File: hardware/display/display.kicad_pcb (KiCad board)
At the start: 2 copper layers, 110 x 70 mm, 58 parts, among them J1 Conn_01x05_Male, J2 CANPWR, J3 CANGND, J4 RJ45, J5 RJ45, J6 Conn_02x03_Odd_Even, J7 DCDC-PWM, J8 DCDC-MEASURES, J9 display, Q1 BSS123, SW1 next, SW2 select, U1 2.048V, U2 AP63200WU, U3 PIC18F27Q84, U4 TLE9250VSJXUMA1, Y1 10Mhz

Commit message: WIP on diaplay PCB.
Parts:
- removed C10, C12: 22µ, Capacitor_SMD:C_1206_3216Metric_Pad1.33x1.80mm_HandSolder
- removed C11, C13, C7: 100nF, Capacitor_SMD:C_0805_2012Metric_Pad1.18x1.45mm_HandSolder
- removed C14: 100nF, local:C_filter_0805
- removed C2, C3: 4.7µ50V, Capacitor_SMD:C_1206_3216Metric_Pad1.33x1.80mm_HandSolder
- removed C4, C8: 100nF50V, Capacitor_SMD:C_0805_2012Metric_Pad1.18x1.45mm_HandSolder
- removed C5, C6: 22pF, Capacitor_THT:C_Disc_D3.8mm_W2.6mm_P2.50mm
- removed C9: 100p, Capacitor_SMD:C_0805_2012Metric_Pad1.18x1.45mm_HandSolder
- removed D1, D2: PMEG4005, Diode_SMD:D_SOD-123
- removed D3: SMBJ16A, Diode_SMD:D_SMB_Handsoldering
- removed F1, F2: MC011014, Fuse:Fuse_2920_7451Metric_Pad2.10x5.45mm_HandSolder
- removed J2: CANPWR, Connector_PinHeader_2.54mm:PinHeader_1x02_P2.54mm_Vertical
- removed J3: CANGND, Connector_PinHeader_2.54mm:PinHeader_1x02_P2.54mm_Vertical
- removed J4, J5: RJ45, local:RJ45_Amphenol_54602-x08_Horizontal_handsolder
- removed J6: Conn_02x03_Odd_Even, Connector_PinHeader_2.54mm:PinHeader_2x03_P2.54mm_Vertical
- removed J7: DCDC-PWM, Connector_PinHeader_2.54mm:PinHeader_2x05_P2.54mm_Vertical
- removed J8: DCDC-MEASURES, Connector_PinHeader_2.54mm:PinHeader_2x05_P2.54mm_Vertical
- removed J9: display, Connector_Harwin:Harwin_M20-7810345_2x03_P2.54mm_Vertical
- removed L1: 10µH, Inductor_SMD:L_12x12mm_H4.5mm
- removed Q1: BSS123, Package_TO_SOT_SMD:SOT-23
- removed R10: 8.1K, Resistor_THT:R_Axial_DIN0309_L9.0mm_D3.2mm_P12.70mm_Horizontal
- removed R11: 4K7, Resistor_SMD:R_0805_2012Metric_Pad1.20x1.40mm_HandSolder
- removed R12: 4K7, Resistor_THT:R_Axial_DIN0309_L9.0mm_D3.2mm_P12.70mm_Horizontal
- removed R13, R4, R5, R8: 10K, Resistor_SMD:R_0805_2012Metric_Pad1.20x1.40mm_HandSolder
- removed R14: 100K, Resistor_SMD:R_0805_2012Metric_Pad1.20x1.40mm_HandSolder
- removed R15, R16: 47k, Resistor_SMD:R_0805_2012Metric_Pad1.20x1.40mm_HandSolder
- removed R17: 22k, Resistor_SMD:R_0805_2012Metric_Pad1.20x1.40mm_HandSolder
- removed R18: 100, Resistor_SMD:R_0805_2012Metric_Pad1.20x1.40mm_HandSolder
- removed R2: 270k, Resistor_SMD:R_0805_2012Metric_Pad1.20x1.40mm_HandSolder
- removed R3, R7: 30k, Resistor_SMD:R_0805_2012Metric_Pad1.20x1.40mm_HandSolder
- removed R6: 157k, Resistor_SMD:R_0805_2012Metric_Pad1.20x1.40mm_HandSolder
- removed R9: 10K, Resistor_THT:R_Axial_DIN0309_L9.0mm_D3.2mm_P12.70mm_Horizontal
- removed SW1: next, Button_Switch_THT:Push_E-Switch_KS01Q01
- removed SW2: select, Button_Switch_THT:Push_E-Switch_KS01Q01
- removed U1: 2.048V, Package_TO_SOT_SMD:SOT-23
- removed U2: AP63200WU, Package_TO_SOT_SMD:TSOT-23-6
- removed U3: PIC18F27Q84, Package_SO:SOIC-28W_7.5x17.9mm_P1.27mm
- removed U4: TLE9250VSJXUMA1, Package_SO:SOIC-8_3.9x4.9mm_P1.27mm
- removed Y1: 10Mhz, Crystal:Crystal_HC18-U_Vertical
- added DI1: MCOB128064JX, LCDdisplays.mod:MCOB128064JX, F.Cu at (112.0, 105.0)
- H1, H2, H3, H4: value MountingHole -> 3.2mm
- J1: value Conn_01x05_Male -> Conn_02x03_Odd_Even; footprint Connector_PinHeader_2.54mm:PinHeader_1x05_P2.54mm_Horizontal -> harwin:M20-8750342
- moved C1 153.5 mm to (232.4, 43.2), turned to 0 degrees
- moved J1 46.6 mm to (140.0, 86.3)
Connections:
- C1 pad 2: Net-(C1-Pad2) -> +5V
- J1 pad 2: /PGD -> unconnected-(J1-Pad2)
- J1 pad 3: /PGC -> GND
- J1 pad 4: GND -> /~{RST_DISP}
- J1 pad 5: /MCLR -> /SDA
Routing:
- net +5V: track 306.6 -> 0.00 mm, vias 3 -> 0
- net BTN_IN: track 96.5 -> 0.00 mm, vias 1 -> 0
- net SDA: track 94.0 -> 0.00 mm, vias 1 -> 0
- net PWM_V: track 69.9 -> 0.00 mm, vias 2 -> 0
- net TH: track 66.2 -> 0.00 mm, vias 2 -> 0
- net /CANL: track 64.9 -> 0.00 mm
- net /PWM_OFF: track 62.8 -> 0.00 mm
- net /CANGND: track 61.5 -> 0.00 mm
- net /CANH: track 59.3 -> 0.00 mm
- net /PWM: track 58.6 -> 0.00 mm
- net /PWM_OK: track 57.2 -> 0.00 mm
- net AL1: track 56.1 -> 0.00 mm, vias 2 -> 0
- net Net-(C14-Pad1): track 55.3 -> 0.00 mm
- net /~{PAC_DOWN}: track 55.2 -> 0.00 mm, vias 2 -> 0
- net AL2: track 55.1 -> 0.00 mm, vias 2 -> 0
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- removed copper zone on F.Cu, net /CANGND
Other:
- outline, holes or cut-outs redrawn

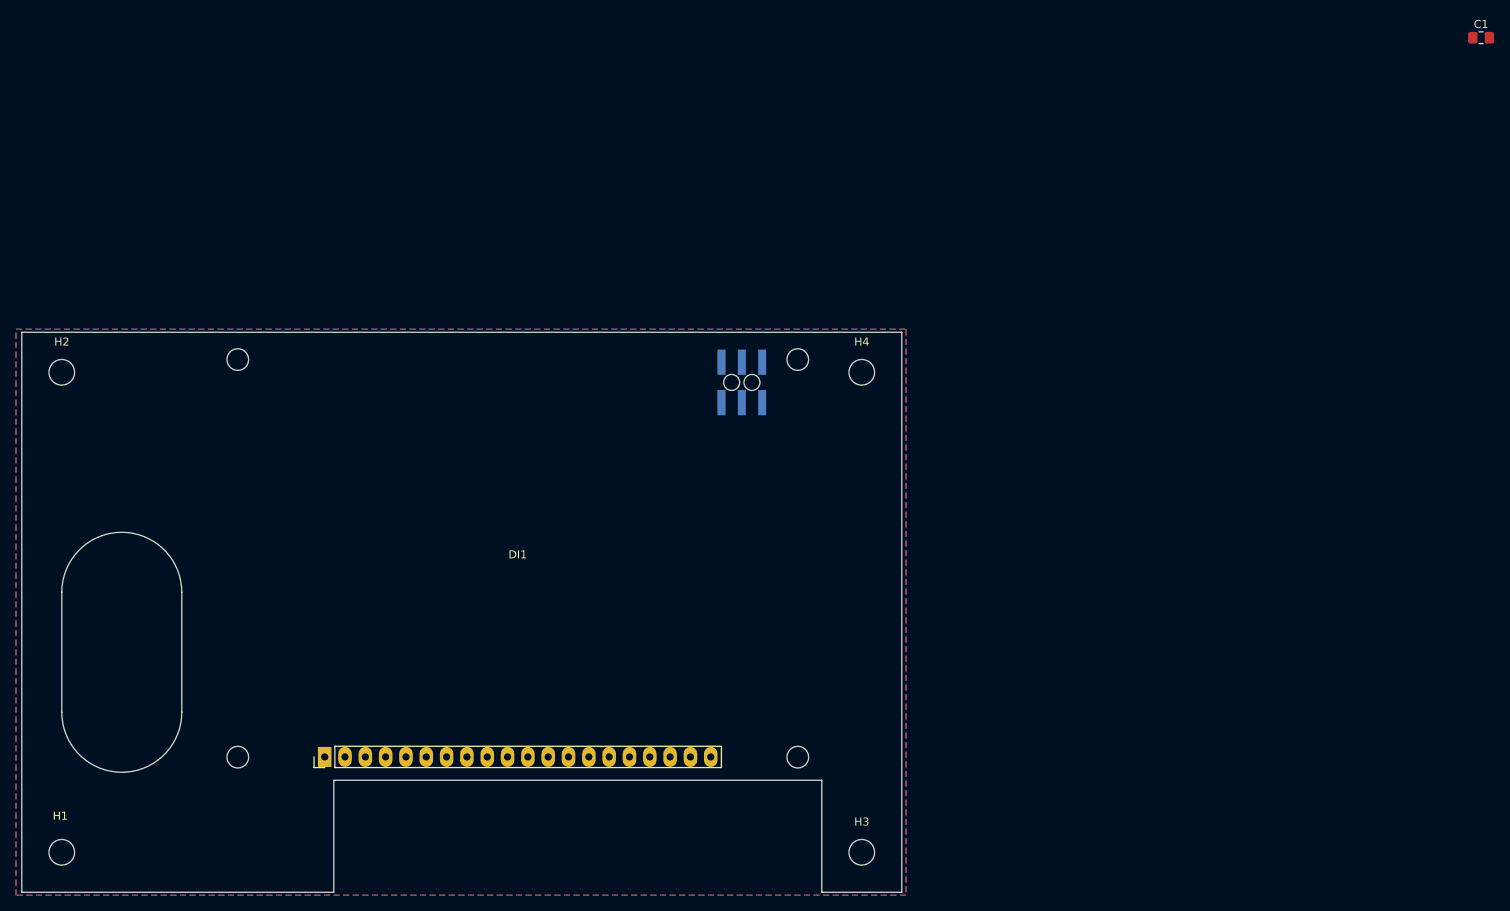
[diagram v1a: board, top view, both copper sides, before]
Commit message: Route display PCB. Adjust control for connector wiring changes.
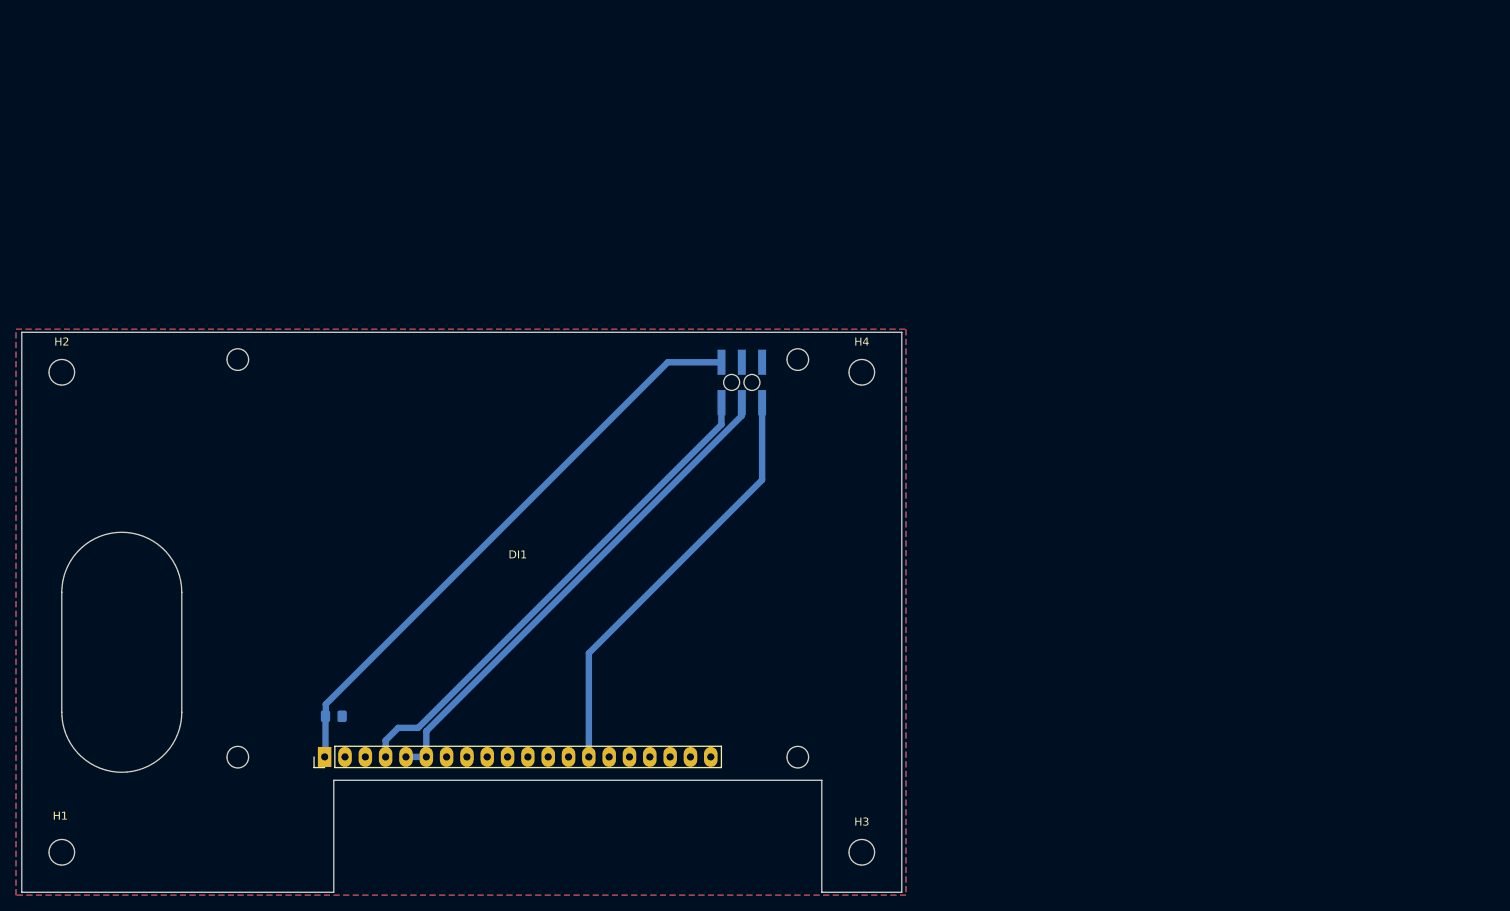
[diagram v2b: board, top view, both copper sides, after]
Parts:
- C1: moved to B.Cu
- moved C1 166.6 mm to (89.0, 128.0), turned to 180 degrees
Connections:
- J1 pad 4: /~{RST_DISP} -> /SCL
- J1 pad 6: /SCL -> /~{RST_DISP}
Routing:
- net +5V: track 0.00 -> 73.8 mm
- net /SDA: track 0.00 -> 63.2 mm
- net /SCL: track 0.00 -> 63.1 mm
- net /~{RST_DISP}: track 0.00 -> 53.3 mm
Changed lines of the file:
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@@
   (paper "A4")
   (layers
-    (0 "F.Cu" signal)
+    (0 "F.Cu" jumper)
     (31 "B.Cu" signal)
     (32 "B.Adhes" user "B.Adhesive")
@@
     (pad "" np_thru_hole circle locked (at 0 0) (size 3.2 3.2) (drill 3.2) (layers *.Cu *.Mask))
   )
-  (footprint "Capacitor_SMD:C_0805_2012Metric_Pad1.18x1.45mm_HandSolder" (layer "F.Cu")
-    (at 232.41 43.18)
-    (descr "Capacitor SMD 0805 (2012 Metric), square (rectangular) end terminal, IPC_7351 nominal with elongated pad for handsoldering. (Body size source: IPC-SM-782 page 76, https://www.pcb-3d.com/wordpress/wp-content/uploads/ipc-sm-782a_amendment_1_and_2.pdf, https://docs.google.com/spreadsheets/d/1BsfQQcO9C6DZCsRaXUlFlo91Tg2WpOkGARC1WS5S8t0/edit?usp=sharing), generated with kicad-footprint-generator")
-    (tags "capacitor handsolder")
-    (property "Sheetfile" "display.kicad_sch")
-    (property "Sheetname" "")
-    (attr smd)
-    (fp_text reference "C1" (at 0 -1.68) (layer "F.SilkS")
-      (effects (font (size 1 1) (thickness 0.15)))
-    )
-    (fp_text value "100nF" (at 0 1.68) (layer "F.Fab")
-      (effects (font (size 1 1) (thickness 0.15)))
-    )
-    (fp_text user "${REFERENCE}" (at 0 0) (layer "F.Fab")
-      (effects (font (size 0.5 0.5) (thickness 0.08)))
-    )
-    (fp_line (start -0.261252 0.735) (end 0.261252 0.735) (layer "F.SilkS") (width 0.12))
-    (fp_line (start -0.261252 -0.735) (end 0.261252 -0.735) (layer "F.SilkS") (width 0.12))
-    (fp_line (start -1.88 0.98) (end -1.88 -0.98) (layer "F.CrtYd") (width 0.05))
-    (fp_line (start 1.88 -0.98) (end 1.88 0.98) (layer "F.CrtYd") (width 0.05))
-    (fp_line (start 1.88 0.98) (end -1.88 0.98) (layer "F.CrtYd") (width 0.05))
-    (fp_line (start -1.88 -0.98) (end 1.88 -0.98) (layer "F.CrtYd") (width 0.05))
-    (fp_line (start 1 -0.625) (end 1 0.625) (layer "F.Fab") (width 0.1))
-    (fp_line (start 1 0.625) (end -1 0.625) (layer "F.Fab") (width 0.1))
-    (fp_line (start -1 0.625) (end -1 -0.625) (layer "F.Fab") (width 0.1))
-    (fp_line (start -1 -0.625) (end 1 -0.625) (layer "F.Fab") (width 0.1))
-    (pad "1" smd roundrect (at -1.0375 0) (size 1.175 1.45) (layers "F.Cu" "F.Paste" "F.Mask") (roundrect_rratio 0.212766)
-      (net 1 "GND") (pintype "passive"))
-    (pad "2" smd roundrect (at 1.0375 0) (size 1.175 1.45) (layers "F.Cu" "F.Paste" "F.Mask") (roundrect_rratio 0.212766)
-      (net 2 "+5V") (pintype "passive"))
-    (model "${KICAD6_3DMODEL_DIR}/Capacitor_SMD.3dshapes/C_0805_2012Metric.wrl"
-      (offset (xyz 0 0 0))
-      (scale (xyz 1 1 1))
-      (rotate (xyz 0 0 0))
-    )
-  )
   (footprint "harwin:M20-8750342" (layer "B.Cu")
     (at 140 86.27 -90)
@@
       (net 1 "GND") (pinfunction "Pin_3") (pintype "passive"))
     (pad "4" smd rect (at 2.525 2.54 270) (size 3.15 1) (layers "B.Cu" "B.Paste" "B.Mask")
-      (net 10 "/~{RST_DISP}") (pinfunction "Pin_4") (pintype "passive"))
+      (net 8 "/SCL") (pinfunction "Pin_4") (pintype "passive"))
     (pad "5" smd rect (at 2.525 0 270) (size 3.15 1) (layers "B.Cu" "B.Paste" "B.Mask")
       (net 9 "/SDA") (pinfunction "Pin_5") (pintype "passive"))
     (pad "6" smd rect (at 2.525 -2.54 270) (size 3.15 1) (layers "B.Cu" "B.Paste" "B.Mask")
-      (net 8 "/SCL") (pinfunction "Pin_6") (pintype "passive"))
+      (net 10 "/~{RST_DISP}") (pinfunction "Pin_6") (pintype "passive"))
+  )
+  (footprint "Capacitor_SMD:C_0805_2012Metric_Pad1.18x1.45mm_HandSolder" (layer "B.Cu")
+    (at 89 128 180)
+    (descr "Capacitor SMD 0805 (2012 Metric), square (rectangular) end terminal, IPC_7351 nominal with elongated pad for handsoldering. (Body size source: IPC-SM-782 page 76, https://www.pcb-3d.com/wordpress/wp-content/uploads/ipc-sm-782a_amendment_1_and_2.pdf, https://docs.google.com/spreadsheets/d/1BsfQQcO9C6DZCsRaXUlFlo91Tg2WpOkGARC1WS5S8t0/edit?usp=sharing), generated with kicad-footprint-generator")
+    (tags "capacitor handsolder")
+    (property "Sheetfile" "display.kicad_sch")
+    (property "Sheetname" "")
+    (attr smd)
+    (fp_text reference "C1" (at 0 1.68) (layer "B.SilkS")
+      (effects (font (size 1 1) (thickness 0.15)) (justify mirror))
+    )
+    (fp_text value "100nF" (at 0 -1.68) (layer "B.Fab")
+      (effects (font (size 1 1) (thickness 0.15)) (justify mirror))
+    )
+    (fp_text user "${REFERENCE}" (at 0 0) (layer "B.Fab")
+      (effects (font (size 0.5 0.5) (thickness 0.08)) (justify mirror))
+    )
+    (fp_line (start -0.261252 -0.735) (end 0.261252 -0.735) (layer "B.SilkS") (width 0.12))
+    (fp_line (start -0.261252 0.735) (end 0.261252 0.735) (layer "B.SilkS") (width 0.12))
+    (fp_line (start -1.88 -0.98) (end -1.88 0.98) (layer "B.CrtYd") (width 0.05))
+    (fp_line (start 1.88 0.98) (end 1.88 -0.98) (layer "B.CrtYd") (width 0.05))
+    (fp_line (start 1.88 -0.98) (end -1.88 -0.98) (layer "B.CrtYd") (width 0.05))
+    (fp_line (start -1.88 0.98) (end 1.88 0.98) (layer "B.CrtYd") (width 0.05))
+    (fp_line (start 1 0.625) (end 1 -0.625) (layer "B.Fab") (width 0.1))
+    (fp_line (start 1 -0.625) (end -1 -0.625) (layer "B.Fab") (width 0.1))
+    (fp_line (start -1 -0.625) (end -1 0.625) (layer "B.Fab") (width 0.1))
+    (fp_line (start -1 0.625) (end 1 0.625) (layer "B.Fab") (width 0.1))
+    (pad "1" smd roundrect (at -1.0375 0 180) (size 1.175 1.45) (layers "B.Cu" "B.Paste" "B.Mask") (roundrect_rratio 0.212766)
+      (net 1 "GND") (pintype "passive"))
+    (pad "2" smd roundrect (at 1.0375 0 180) (size 1.175 1.45) (layers "B.Cu" "B.Paste" "B.Mask") (roundrect_rratio 0.212766)
+      (net 2 "+5V") (pintype "passive"))
+    (model "${KICAD6_3DMODEL_DIR}/Capacitor_SMD.3dshapes/C_0805_2012Metric.wrl"
+      (offset (xyz 0 0 0))
+      (scale (xyz 1 1 1))
+      (rotate (xyz 0 0 0))
+    )
   )
   (gr_arc (start 55 112.5) (mid 62.5 105) (end 70 112.5) (layer "Edge.Cuts") (width 0.1))
@@
       (xy 160 80)
     ) (layer "Edge.Cuts") (width 0.1) (fill none))
+  (segment (start 88 127.9625) (end 87.9625 128) (width 0.8) (layer "B.Cu") (net 2))
+  (segment (start 87.9625 132.98) (end 87.8625 133.08) (width 0.8) (layer "B.Cu") (net 2))
+  (segment (start 87.9625 128) (end 87.9625 132.98) (width 0.8) (layer "B.Cu") (net 2))
+  (segment (start 130.755 83.745) (end 88 126.5) (width 0.8) (layer "B.Cu") (net 2))
+  (segment (start 88 126.5) (end 88 127.9625) (width 0.8) (layer "B.Cu") (net 2))
+  (segment (start 137.46 83.745) (end 130.755 83.745) (width 0.8) (layer "B.Cu") (net 2))
+  (segment (start 137.46 88.795) (end 137.46 91.54) (width 0.8) (layer "B.Cu") (net 8))
+  (segment (start 99.5525 129.4475) (end 97.0525 129.4475) (width 0.8) (layer "B.Cu") (net 8))
+  (segment (start 95.4825 131.0175) (end 95.4825 133.08) (width 0.8) (layer "B.Cu") (net 8))
+  (segment (start 97.0525 129.4475) (end 95.4825 131.0175) (width 0.8) (layer "B.Cu") (net 8))
+  (segment (start 137.46 91.54) (end 99.5525 129.4475) (width 0.8) (layer "B.Cu") (net 8))
+  (segment (start 140 88.795) (end 140 90.428356) (width 0.8) (layer "B.Cu") (net 9))
+  (segment (start 100.5625 129.865856) (end 100.5625 133.08) (width 0.8) (layer "B.Cu") (net 9))
+  (segment (start 140 90.428356) (end 100.5625 129.865856) (width 0.8) (layer "B.Cu") (net 9))
+  (segment (start 98.0225 133.08) (end 100.5625 133.08) (width 0.8) (layer "B.Cu") (net 9))
+  (segment (start 142.54 98.46) (end 120.8825 120.1175) (width 0.8) (layer "B.Cu") (net 10))
+  (segment (start 120.8825 120.1175) (end 120.8825 133.08) (width 0.8) (layer "B.Cu") (net 10))
+  (segment (start 142.54 88.795) (end 142.54 98.46) (width 0.8) (layer "B.Cu") (net 10))
   (zone (net 1) (net_name "GND") (layers F&B.Cu) (hatch edge 0.508)
     (connect_pads (clearance 0.21))
